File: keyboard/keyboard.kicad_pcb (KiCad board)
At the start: 2 copper layers, 134.3 x 100.9 mm, 42 parts

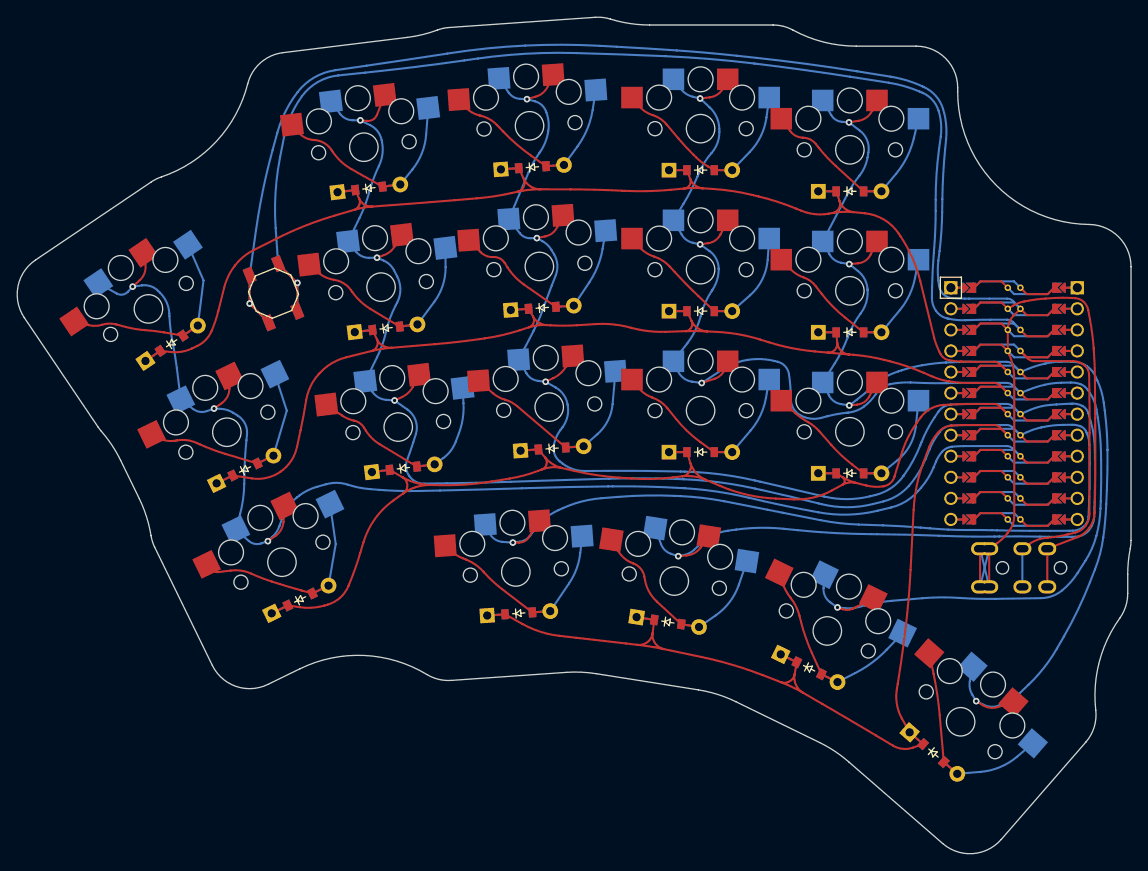
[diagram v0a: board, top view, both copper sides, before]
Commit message: Add tenting puck, reroute traces around
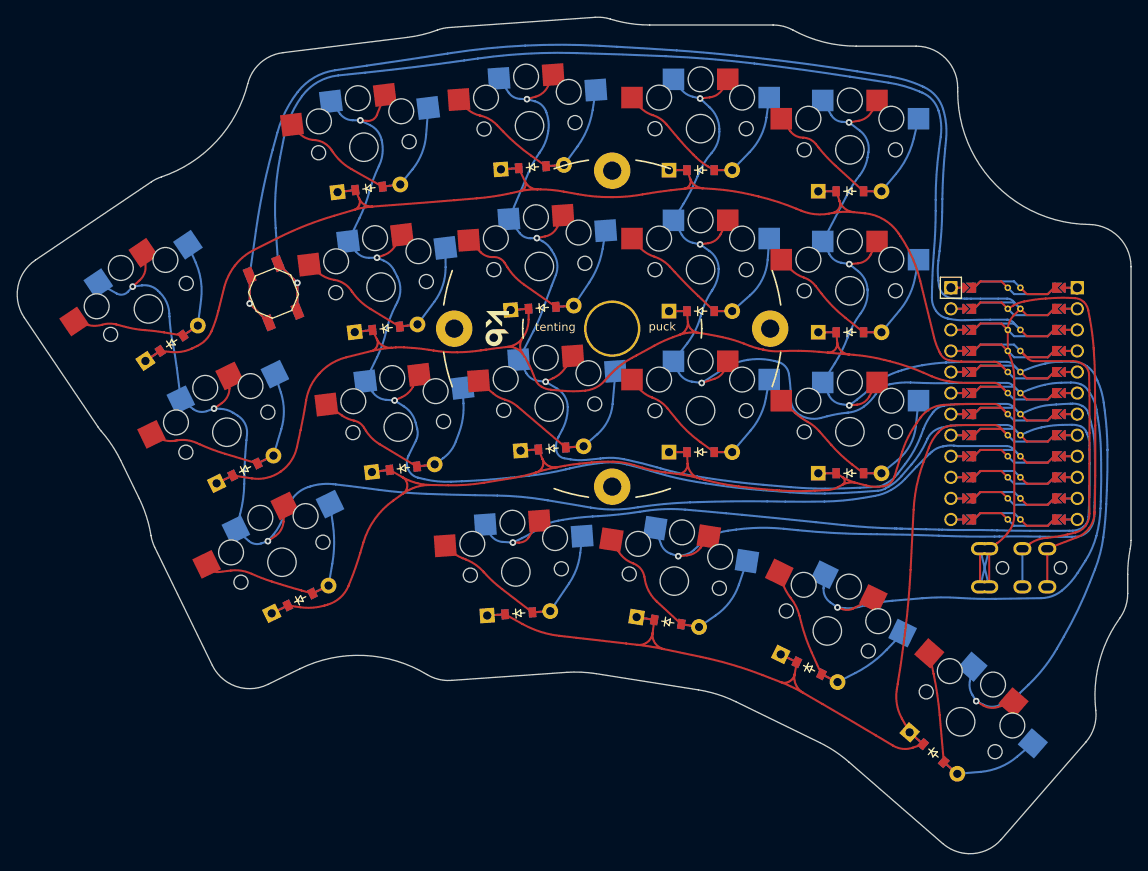
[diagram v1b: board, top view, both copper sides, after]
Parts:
- added REF**: Tenting Puck, library:TentingPuck, F.Cu at (217.4, 107.8)
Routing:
- net D0: track 146.1 -> 153.8 mm
- net F7: track 249.3 -> 243.5 mm
- net B1: track 160.8 -> 155.7 mm
- net F6: track 217.7 -> 216.1 mm
- net D4: track 146.5 -> 145.6 mm
- net D1: track 165.1 -> 164.5 mm

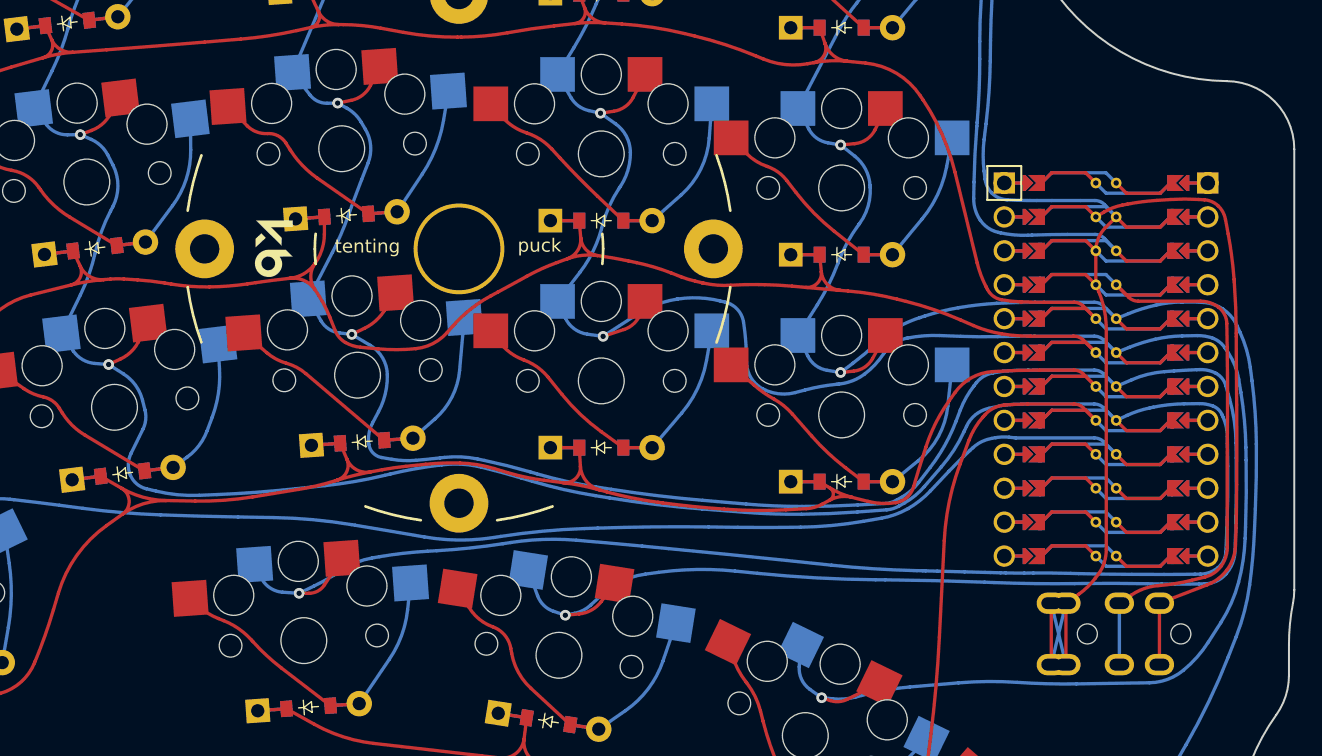
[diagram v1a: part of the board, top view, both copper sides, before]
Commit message: Change JLC order number position to barcode position
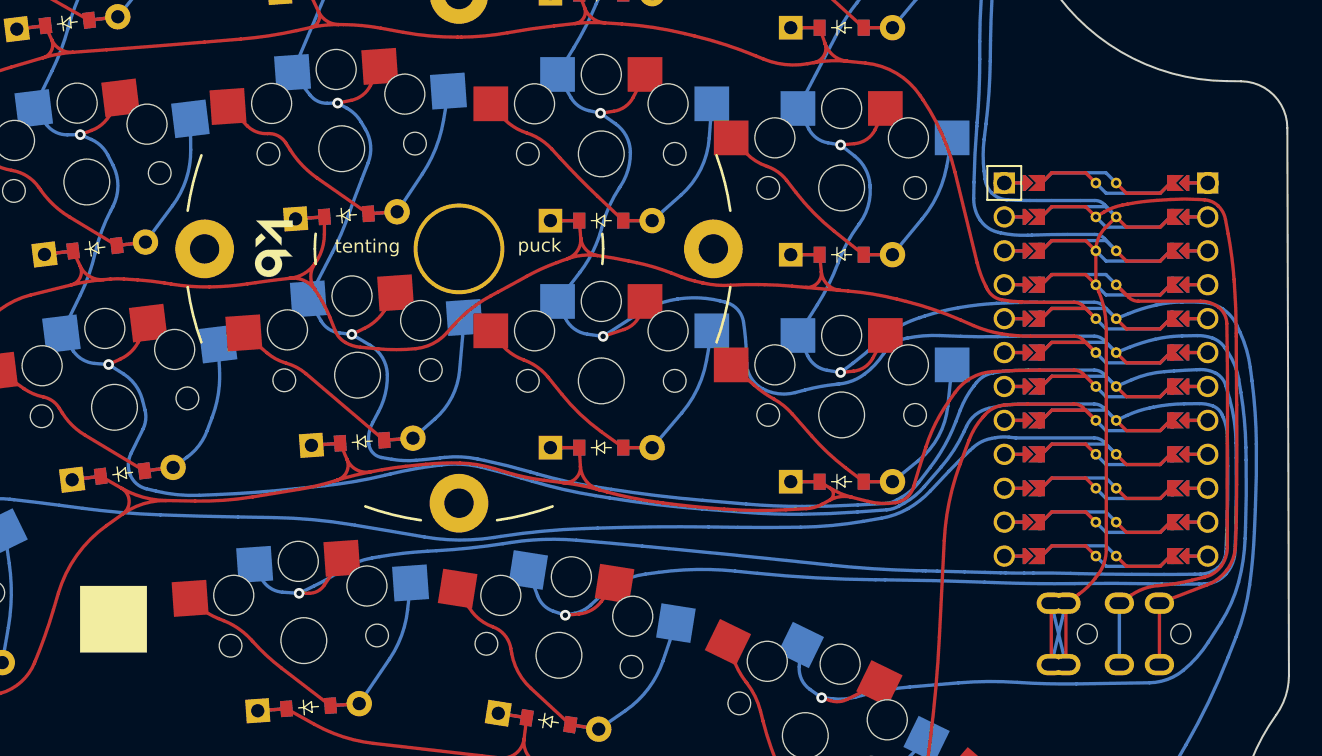
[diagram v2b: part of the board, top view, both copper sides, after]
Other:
- board size 134.3 x 100.9 mm -> 133.9 x 100.9 mm
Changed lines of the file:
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@@
 	(layers
 		(0 "F.Cu" signal)
-		(31 "B.Cu" signal)
+		(31 "B.Cu" jumper)
 		(32 "B.Adhes" user "B.Adhesive")
 		(33 "F.Adhes" user "F.Adhesive")
@@
 	)
 	(setup
+		(stackup
+			(layer "F.SilkS"
+				(type "Top Silk Screen")
+			)
+			(layer "F.Paste"
+				(type "Top Solder Paste")
+			)
+			(layer "F.Mask"
+				(type "Top Solder Mask")
+				(thickness 0.01)
+			)
+			(layer "F.Cu"
+				(type "copper")
+				(thickness 0.035)
+			)
+			(layer "dielectric 1"
+				(type "core")
+				(thickness 1.51)
+				(material "FR4")
+				(epsilon_r 4.5)
+				(loss_tangent 0.02)
+			)
+			(layer "B.Cu"
+				(type "copper")
+				(thickness 0.035)
+			)
+			(layer "B.Mask"
+				(type "Bottom Solder Mask")
+				(thickness 0.01)
+			)
+			(layer "B.Paste"
+				(type "Bottom Solder Paste")
+			)
+			(layer "B.SilkS"
+				(type "Bottom Silk Screen")
+			)
+			(copper_finish "None")
+			(dielectric_constraints no)
+		)
 		(pad_to_mask_clearance 0.05)
 		(allow_soldermask_bridges_in_footprints no)
@@
 		)
 	)
+	(gr_rect
+		(start 189 133)
+		(end 194 138)
+		(stroke
+			(width 0)
+			(type solid)
+		)
+		(fill solid)
+		(layer "B.SilkS")
+	)
+	(gr_rect
+		(start 189 133)
+		(end 194 138)
+		(stroke
+			(width 0)
+			(type solid)
+		)
+		(fill solid)
+		(layer "F.SilkS")
+	)
 	(gr_line
 		(start 264.280869 169.350898)
@@
 	)
 	(gr_arc
-		(start 279.531797 137.386311)
-		(mid 279.607807 135.828575)
-		(end 279.835114 134.28564)
+		(start 264.280213 169.351652)
+		(mid 260.855448 171.059177)
+		(end 257.22637 169.844905)
 		(stroke
 			(width 0.15)
@@
 	)
 	(gr_arc
-		(start 264.280213 169.351652)
-		(mid 260.855448 171.059177)
-		(end 257.22637 169.844905)
+		(start 275.950871 95.20996)
+		(mid 278.395753 96.245585)
+		(end 279.410228 98.699346)
 		(stroke
 			(width 0.15)
-			(type solid)
+			(type default)
 		)
 		(layer "Edge.Cuts")
@@
 	)
 	(gr_line
+		(start 275.950871 95.20996)
+		(end 274.880137 95.19753)
+		(stroke
+			(width 0.15)
+			(type default)
+		)
+		(layer "Edge.Cuts")
+	)
+	(gr_line
 		(start 162.208835 134.115432)
 		(end 169.157095 148.361475)
@@
 	(gr_line
 		(start 279.531796 139.697301)
-		(end 279.531796 137.38631)
+		(end 279.410228 98.699346)
 		(stroke
 			(width 0.15)
@@
 		(layer "Edge.Cuts")
 	)
-	(gr_line
-		(start 279.931796 133.297301)
-		(end 279.931796 100.297301)
-		(stroke
-			(width 0.15)
-			(type solid)
-		)
-		(layer "Edge.Cuts")
-	)
 	(gr_arc
 		(start 215.322679 70.21831)
@@
 		(stroke
 			(width 0.15)
-			(type solid)
-		)
-		(layer "Edge.Cuts")
-	)
-	(gr_arc
-		(start 274.880137 95.19753)
-		(mid 278.455091 96.708188)
-		(end 279.931796 100.297301)
-		(stroke
-			(width 0.15)
-			(type solid)
-		)
-		(layer "Edge.Cuts")
-	)
-	(gr_arc
-		(start 279.931796 133.297301)
-		(mid 279.907568 133.793829)
-		(end 279.835114 134.28564)
-		(stroke
-			(width 0.15)
